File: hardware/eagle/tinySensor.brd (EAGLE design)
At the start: 160 x 100 mm, 0 parts

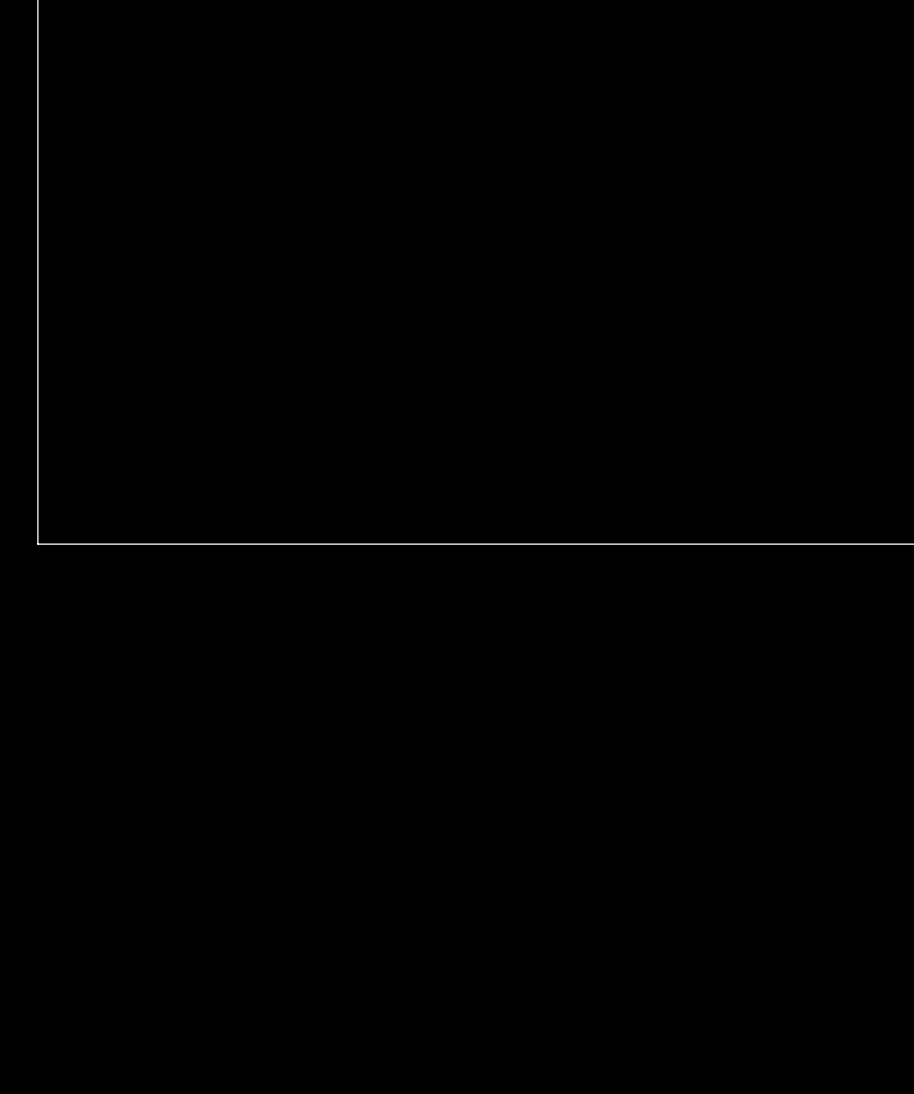
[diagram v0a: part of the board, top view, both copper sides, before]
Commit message: Schematics redrawn, work in progress
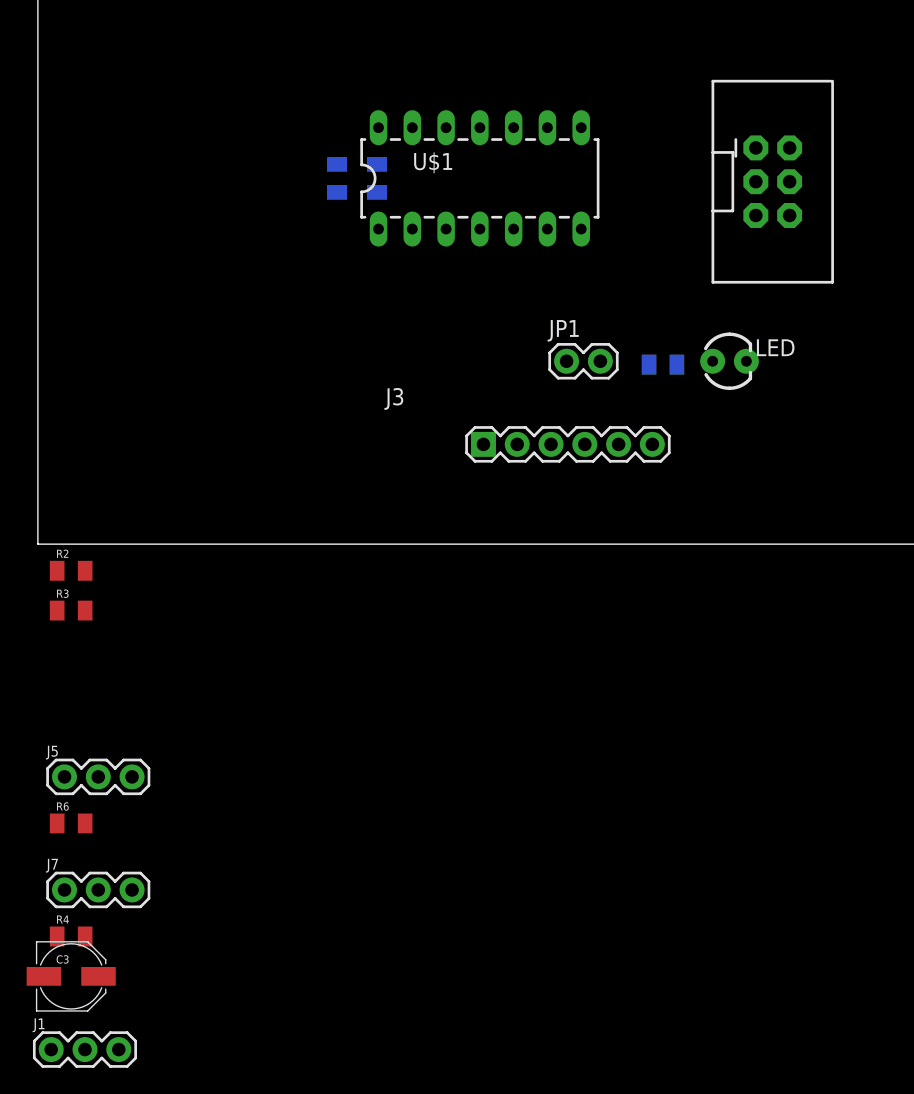
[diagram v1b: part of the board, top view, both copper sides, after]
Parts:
- added C1: 100nF, 0SBLib:R0805
- added C2: 10uF, 0SBLib:R0805
- added C3: 1uF, rcl:PANASONIC_C
- added J1, J5, J7: (no value), 0SBLib:1X03
- added J3: (no value), SparkFun-Connectors:1X06
- added J6: (no value), SparkFun-Connectors:2X3-SHROUDED
- added JP1: (no value), SparkFun-Retired:1X02
- added LED: (no value), 0SBLib:LED3MM
- added R1: 1k, 0SBLib:R0805
- added R2, R3, R6: 4.7k, 0SBLib:R0805
- added R4: 75, 0SBLib:R0805
- added U$1: ATTINY84ATTINY84-20PU, SparkFun-DigitalIC:DIL14
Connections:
- new net ANALOG_SENSOR: J7.2, R4.2, U$1.13
- new net AUX: U$1.5
- new net BATTERY_CHECKER: U$1.12
- new net GND: C1.1, C2.1, C3.-, J1.1, J3.2, J3.6, J5.2, J6.6, J7.1, LED.K, U$1.14
- new net LED_OUT: JP1.1, U$1.3
- new net MISO: J6.1, U$1.8
- new net N$1: JP1.2, R1.1
- new net N$2: LED.A, R1.2
- new net N$4: C3.+, R4.1
- new net ONEWIRE: J5.1, R6.1, U$1.10
- new net PWM_OUT: U$1.6
- new net RESET: J6.5, U$1.4
- new net SCL/SCK: J6.3, U$1.9
- new net SCL_SCK: J3.3, R3.1
- new net SDA/MOSI: J3.4, J6.4, R2.1, U$1.7
- new net SENSOR_VCC: J3.1, J5.3, J7.3, R2.2, R3.2, R6.2, U$1.11
- new net TX_RADIO: J1.3, U$1.2
- new net VCC: C1.2, C2.2, J1.2, J6.2, U$1.1
